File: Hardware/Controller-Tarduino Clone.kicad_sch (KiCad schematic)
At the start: 20 parts, among them J1 Conn_01x07_Male, J2 Conn_01x04_Male, J3 Conn_01x02_Male, J4 Conn_01x02_Male, J5 Conn_01x02_Male, J6 Conn_01x02_Male, J7 Conn_01x08_Male, J8 QWIIC_Vertical, J9 QWIIC_Stackable, SW1 SW_Push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

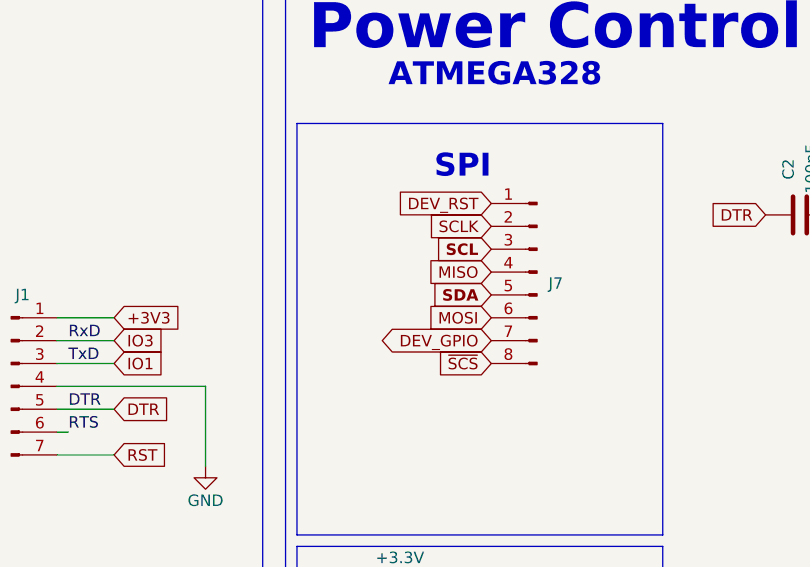
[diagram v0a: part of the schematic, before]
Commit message: Working on Controller-Tarduino Clone
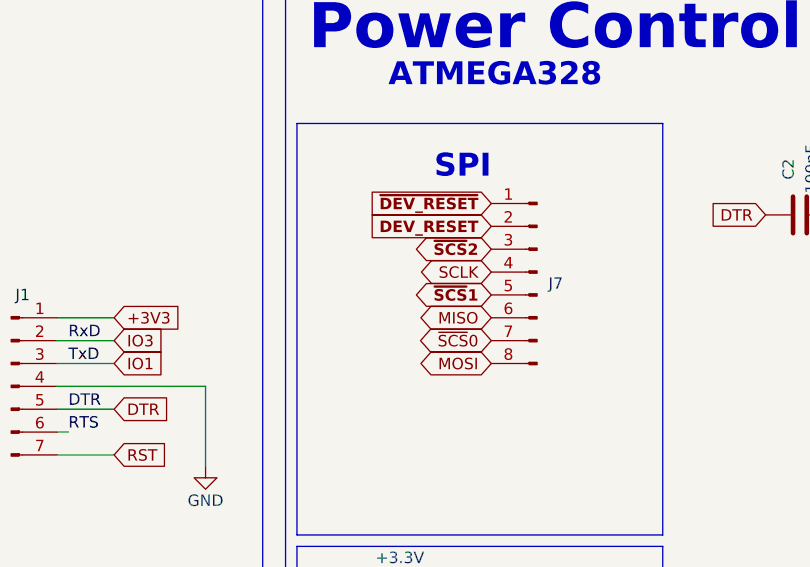
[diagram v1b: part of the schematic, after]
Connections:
- net ~{SCS} is gone; now on net MOSI: J7.8 (Pin_8)
- net MISO: now also J7.6 (Pin_6); no longer J7.4 (Pin_4)
- net MOSI: no longer J7.6 (Pin_6)
- net SCL: no longer J7.3 (Pin_3)
- net SCLK: now also J7.4 (Pin_4); no longer J7.2 (Pin_2)
- net SDA: no longer J7.5 (Pin_5)
- net DEV_GPIO renamed ~{SCS}0
- net DEV_RST renamed ~{DEV_RESET}
- new net DEV_RESET: J7.2 (Pin_2)
- new net ~{SCS}1: J7.5 (Pin_5)
- new net ~{SCS}2: J7.3 (Pin_3)
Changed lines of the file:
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@@
     )
   )
-  (global_label "SDA" (shape input) (at 118.11 50.8 180) (fields_autoplaced)
-    (effects (font (size 1.27 1.27) bold) (justify right))
-    (property "Intersheet References" "${INTERSHEET_REFS}" (id 0) (at 111.9384 50.673 0)
-      (effects (font (size 1.27 1.27) bold) (justify right) hide)
-    )
-  )
-  (global_label "DEV_RST" (shape input) (at 118.11 40.64 180) (fields_autoplaced)
-    (effects (font (size 1.27 1.27)) (justify right))
-    (property "Intersheet References" "${INTERSHEET_REFS}" (id 0) (at 107.7745 40.5606 0)
-      (effects (font (size 1.27 1.27)) (justify right) hide)
+  (global_label "MOSI" (shape bidirectional) (at 118.11 58.42 180) (fields_autoplaced)
+    (effects (font (size 1.27 1.27)) (justify right))
+    (property "Intersheet References" "${INTERSHEET_REFS}" (id 0) (at 111.1007 58.3406 0)
+      (effects (font (size 1.27 1.27)) (justify right) hide)
+    )
+  )
+  (global_label "~{DEV_RESET}" (shape input) (at 118.11 40.64 180) (fields_autoplaced)
+    (effects (font (size 1.27 1.27) (thickness 0.254) bold) (justify right))
+    (property "Intersheet References" "${INTERSHEET_REFS}" (id 0) (at 105.286 40.513 0)
+      (effects (font (size 1.27 1.27) (thickness 0.254) bold) (justify right) hide)
     )
   )
@@
     )
   )
+  (global_label "SCLK" (shape bidirectional) (at 118.11 48.26 180) (fields_autoplaced)
+    (effects (font (size 1.27 1.27)) (justify right))
+    (property "Intersheet References" "${INTERSHEET_REFS}" (id 0) (at 110.9193 48.1806 0)
+      (effects (font (size 1.27 1.27)) (justify right) hide)
+    )
+  )
   (global_label "SCL" (shape input) (at 111.76 93.98 180) (fields_autoplaced)
     (effects (font (size 1.27 1.27) (thickness 0.254) bold) (justify right))
@@
     )
   )
+  (global_label "~{SCS}1" (shape bidirectional) (at 118.11 50.8 180) (fields_autoplaced)
+    (effects (font (size 1.27 1.27) (thickness 0.254) bold) (justify right))
+    (property "Intersheet References" "${INTERSHEET_REFS}" (id 0) (at 110.6079 50.673 0)
+      (effects (font (size 1.27 1.27) (thickness 0.254) bold) (justify right) hide)
+    )
+  )
   (global_label "Vout" (shape input) (at 24.13 102.87 180) (fields_autoplaced)
     (effects (font (size 1.27 1.27)) (justify right))
@@
     (property "Intersheet References" "${INTERSHEET_REFS}" (id 0) (at 234.5207 60.8806 0)
       (effects (font (size 1.27 1.27)) (justify left) hide)
+    )
+  )
+  (global_label "MISO" (shape bidirectional) (at 118.11 53.34 180) (fields_autoplaced)
+    (effects (font (size 1.27 1.27)) (justify right))
+    (property "Intersheet References" "${INTERSHEET_REFS}" (id 0) (at 111.1007 53.2606 0)
+      (effects (font (size 1.27 1.27)) (justify right) hide)
     )
   )
@@
     )
   )
+  (global_label "DEV_RESET" (shape input) (at 118.11 43.18 180) (fields_autoplaced)
+    (effects (font (size 1.27 1.27) (thickness 0.254) bold) (justify right))
+    (property "Intersheet References" "${INTERSHEET_REFS}" (id 0) (at 105.286 43.053 0)
+      (effects (font (size 1.27 1.27) (thickness 0.254) bold) (justify right) hide)
+    )
+  )
   (global_label "Vsec" (shape input) (at 24.13 148.59 180) (fields_autoplaced)
     (effects (font (size 1.27 1.27)) (justify right))
@@
     )
   )
-  (global_label "SCL" (shape input) (at 118.11 45.72 180) (fields_autoplaced)
-    (effects (font (size 1.27 1.27) (thickness 0.254) bold) (justify right))
-    (property "Intersheet References" "${INTERSHEET_REFS}" (id 0) (at 111.9989 45.593 0)
-      (effects (font (size 1.27 1.27) (thickness 0.254) bold) (justify right) hide)
-    )
-  )
   (global_label "D6" (shape input) (at 220.98 106.68 0) (fields_autoplaced)
     (effects (font (size 1.27 1.27)) (justify left))
@@
     )
   )
-  (global_label "SCLK" (shape input) (at 118.11 43.18 180) (fields_autoplaced)
-    (effects (font (size 1.27 1.27)) (justify right))
-    (property "Intersheet References" "${INTERSHEET_REFS}" (id 0) (at 110.9193 43.1006 0)
-      (effects (font (size 1.27 1.27)) (justify right) hide)
-    )
-  )
-  (global_label "MOSI" (shape input) (at 118.11 53.34 180) (fields_autoplaced)
-    (effects (font (size 1.27 1.27)) (justify right))
-    (property "Intersheet References" "${INTERSHEET_REFS}" (id 0) (at 111.1007 53.2606 0)
+  (global_label "~{SCS}0" (shape bidirectional) (at 118.11 55.88 180) (fields_autoplaced)
+    (effects (font (size 1.27 1.27)) (justify right))
+    (property "Intersheet References" "${INTERSHEET_REFS}" (id 0) (at 110.7983 55.8006 0)
       (effects (font (size 1.27 1.27)) (justify right) hide)
     )
@@
     )
   )
-  (global_label "MISO" (shape input) (at 118.11 48.26 180) (fields_autoplaced)
-    (effects (font (size 1.27 1.27)) (justify right))
-    (property "Intersheet References" "${INTERSHEET_REFS}" (id 0) (at 111.1007 48.1806 0)
-      (effects (font (size 1.27 1.27)) (justify right) hide)
-    )
-  )
   (global_label "SDA" (shape input) (at 151.13 129.54 0) (fields_autoplaced)
     (effects (font (size 1.27 1.27)) (justify left))
@@
     )
   )
-  (global_label "DEV_GPIO" (shape bidirectional) (at 118.11 55.88 180) (fields_autoplaced)
-    (effects (font (size 1.27 1.27)) (justify right))
-    (property "Intersheet References" "${INTERSHEET_REFS}" (id 0) (at 106.7464 55.8006 0)
-      (effects (font (size 1.27 1.27)) (justify right) hide)
-    )
-  )
   (global_label "RESET" (shape input) (at 233.68 86.36 0) (fields_autoplaced)
     (effects (font (size 1.27 1.27)) (justify left))
@@
     )
   )
-  (global_label "~{SCS}" (shape input) (at 118.11 58.42 180) (fields_autoplaced)
-    (effects (font (size 1.27 1.27)) (justify right))
-    (property "Intersheet References" "${INTERSHEET_REFS}" (id 0) (at 112.0079 58.3406 0)
-      (effects (font (size 1.27 1.27)) (justify right) hide)
-    )
-  )
   (global_label "UD+" (shape input) (at 26.67 34.29 180) (fields_autoplaced)
     (effects (font (size 1.27 1.27)) (justify right))
@@
     )
   )
+  (global_label "~{SCS}2" (shape bidirectional) (at 118.11 45.72 180) (fields_autoplaced)
+    (effects (font (size 1.27 1.27) (thickness 0.254) bold) (justify right))
+    (property "Intersheet References" "${INTERSHEET_REFS}" (id 0) (at 110.6079 45.593 0)
+      (effects (font (size 1.27 1.27) (thickness 0.254) bold) (justify right) hide)
+    )
+  )
